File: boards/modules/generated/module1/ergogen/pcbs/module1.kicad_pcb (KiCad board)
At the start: 2 copper layers, 75.2 x 75.2 mm, 19 parts

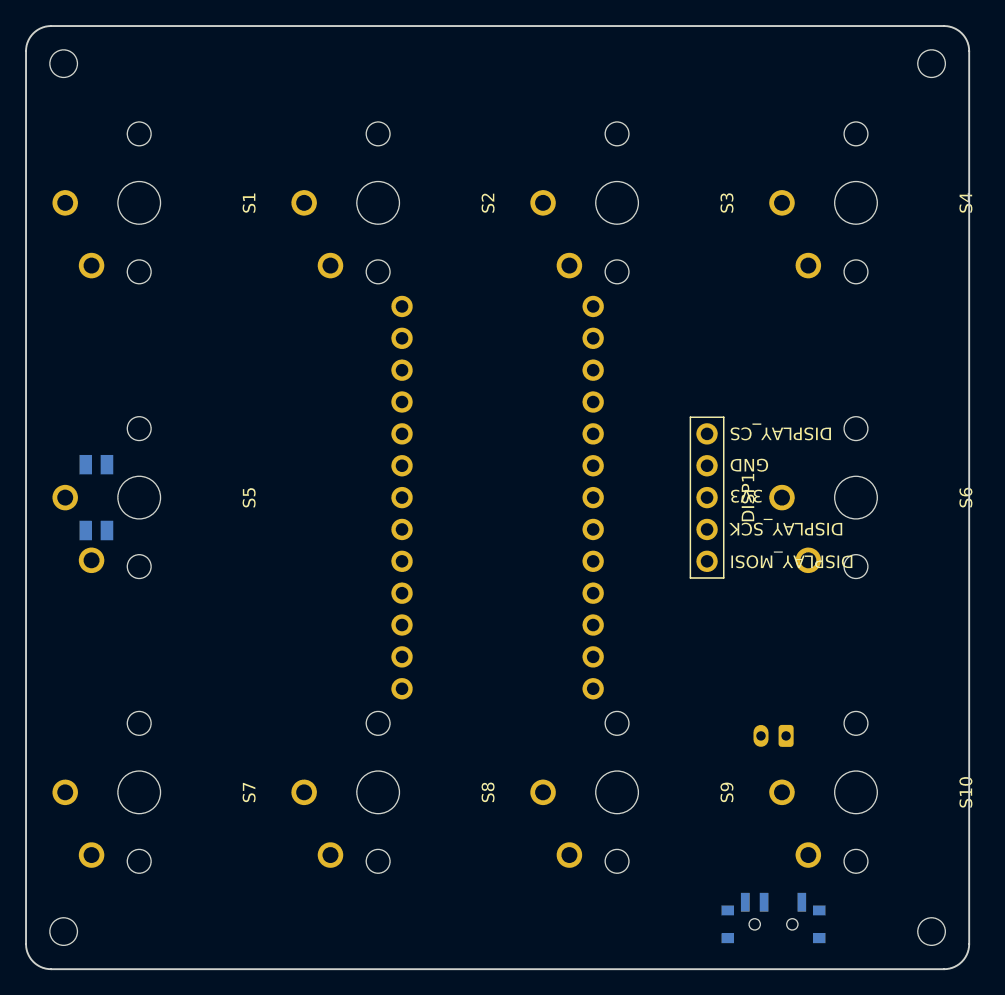
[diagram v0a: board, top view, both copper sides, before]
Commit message: Route every module with broad ground planes and retain TPS43 with top display
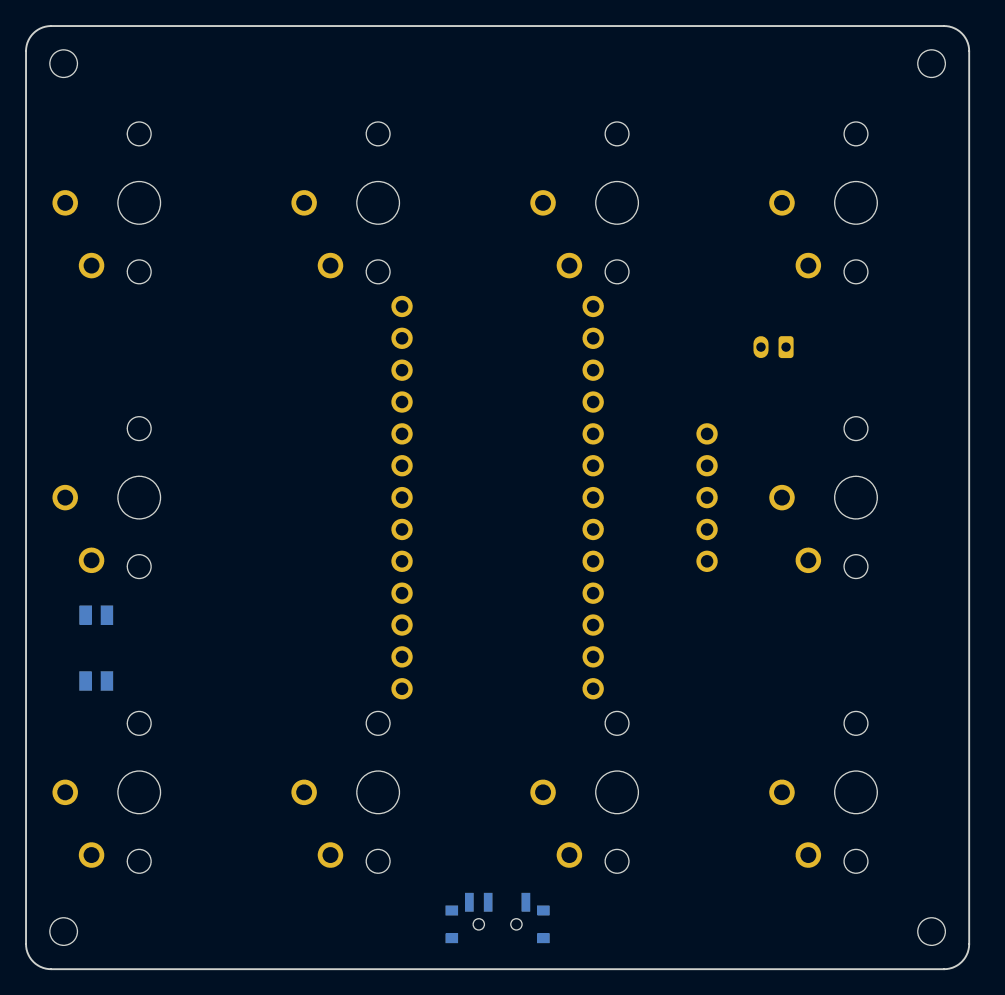
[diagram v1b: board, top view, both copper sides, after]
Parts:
- DISP1: footprint ceoloide:display_nice_view -> display_nice_view
- JST1: footprint ceoloide:battery_connector_jst_ph_2 -> battery_connector_jst_ph_2
- MCU1: footprint ceoloide:mcu_nice_nano -> mcu_nice_nano
- MH1, MH2, MH3, MH4: footprint ceoloide:mounting_hole_npth -> mounting_hole_npth
- PWR1: footprint ceoloide:power_switch_smd_side -> power_switch_smd_side
- RST1: footprint ceoloide:reset_switch_smd_side -> reset_switch_smd_side
- S1, S10, S2, S3, S4, S5, S6, S7, S8, S9: footprint ceoloide:switch_choc_v1_v2 -> switch_choc_v1_v2
- moved JST1 31.0 mm to (122.0, 88.0)
- moved PWR1 22.0 mm to (100.0, 134.0)
- moved RST1 12.0 mm to (68.0, 112.0)
